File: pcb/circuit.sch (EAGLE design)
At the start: 148 parts, among them IC1 MCP1612-ADJI/MS, IC2 MCP73833-AMI/UN-ND, IC3 WE-TVS, IC4 MCP3423, IC5 ATWINC1510-MR210PB1952-ND, IC6 MAX3378EEUD, IC7 RN4870, IC8 ATSAML22N18A, J1 22-05-7038-03, J2 22-05-7038-03, Q1 ECX-1210, T1 PMOS, T10 NMOSSOT323, T11 NMOSSOT323, T12 NMOSSOT323, T2 NMOSSOT323, T3 NMOSSOT323, T4 NMOSSOT323, T5 NMOSSOT323, T6 NMOSSOT323, T7 NMOSSOT323, T8 NMOSSOT323, T9 NMOSSOT323, X1 USB2-MICRO, X10 2.5MM-AUDIO-JACK-MONONO_DRILL, X11 2.5MM-AUDIO-JACK-MONONO_DRILL, X12 2.5MM-AUDIO-JACK-MONONO_DRILL, X13 2.5MM-AUDIO-JACK-MONONO_DRILL, X14 MOLEX_1MM_FPC, X15 IGRID-20, X2 B3S-1000, X4 2.5MM-AUDIO-JACK-MONODRILL, X5 2.5MM-AUDIO-JACK-MONODRILL, X6 2.5MM-AUDIO-JACK-MONODRILL, X7 2.5MM-AUDIO-JACK-MONODRILL, X8 2.5MM-AUDIO-JACK-MONODRILL, X9 2.5MM-AUDIO-JACK-MONONO_DRILL

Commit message: routing finished
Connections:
- net SENSOR_IN_0: now also IC8.PB4; no longer IC8.PB5
- net SENSOR_IN_5: now also IC8.PB5; no longer IC8.PB4
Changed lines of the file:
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@@
 <net name="SENSOR_IN_0" class="0">
 <segment>
-<label x="48.26" y="111.76" size="0.889" layer="95" rot="R180" xref="yes"/>
-<pinref part="IC8" gate="G$1" pin="PB5"/>
-<wire x1="48.26" y1="111.76" x2="55.88" y2="111.76" width="0.1524" layer="91"/>
+<label x="48.26" y="114.3" size="0.889" layer="95" rot="R180" xref="yes"/>
+<wire x1="48.26" y1="114.3" x2="55.88" y2="114.3" width="0.1524" layer="91"/>
+<pinref part="IC8" gate="G$1" pin="PB4"/>
 </segment>
 </net>
@@
 <net name="SENSOR_IN_5" class="0">
 <segment>
-<label x="48.26" y="114.3" size="0.889" layer="95" rot="R180" xref="yes"/>
-<wire x1="48.26" y1="114.3" x2="55.88" y2="114.3" width="0.1524" layer="91"/>
-<pinref part="IC8" gate="G$1" pin="PB4"/>
+<label x="48.26" y="111.76" size="0.889" layer="95" rot="R180" xref="yes"/>
+<pinref part="IC8" gate="G$1" pin="PB5"/>
+<wire x1="48.26" y1="111.76" x2="55.88" y2="111.76" width="0.1524" layer="91"/>
 </segment>
 </net>

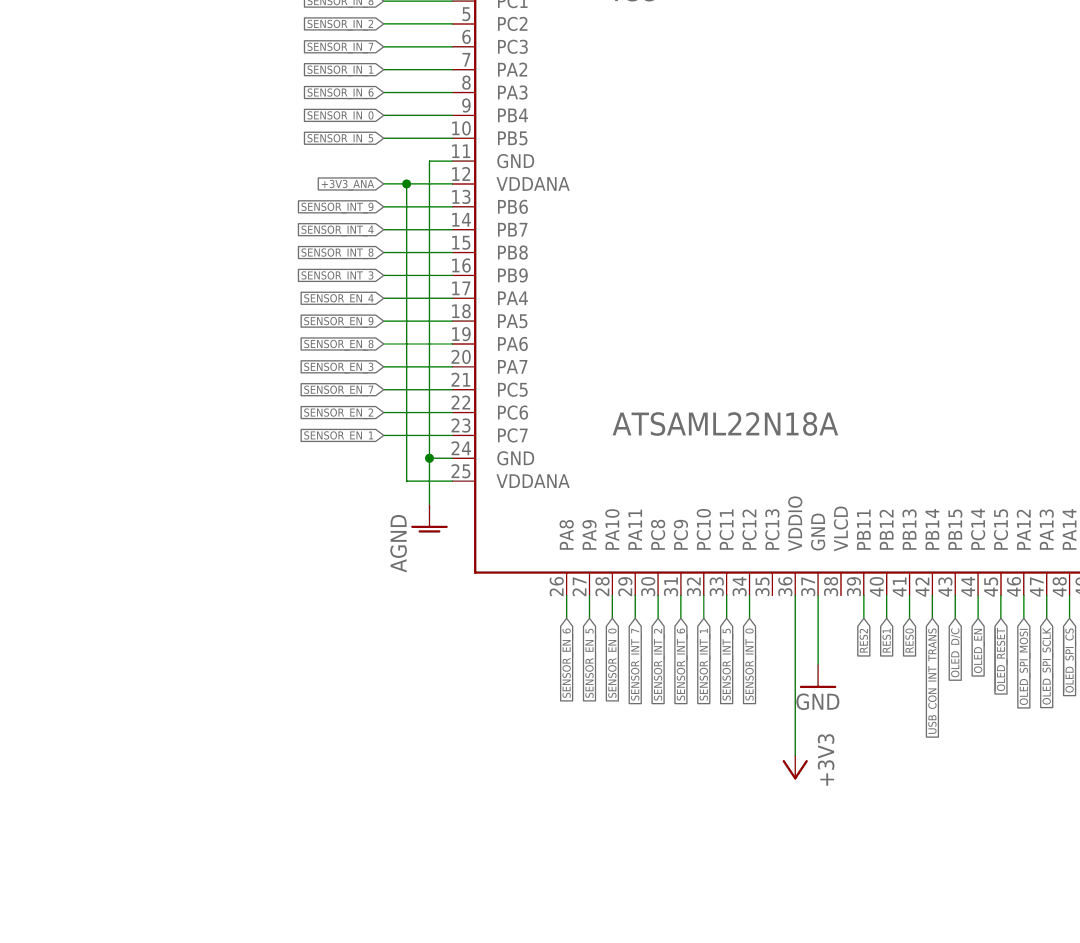
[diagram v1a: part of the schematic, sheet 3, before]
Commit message: Added Internal NTC
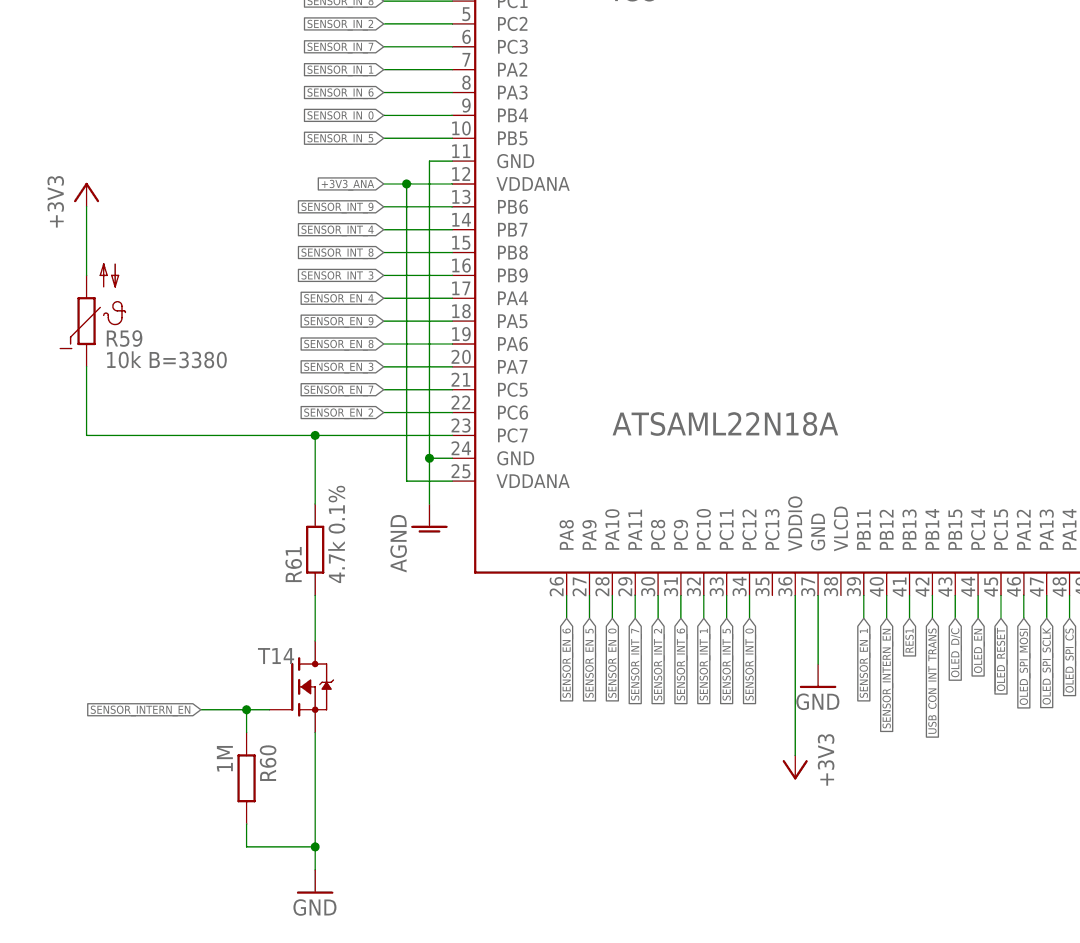
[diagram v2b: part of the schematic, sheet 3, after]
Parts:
- removed J1: 22-05-7038-03, con-molex:22-05-7038-03
- removed JP5: (no value), thermo:JP3
- added J3: 22-05-7048-04, con-molex:22-05-7048-04
- added JP2: (no value), thermo:JP3
- added R58: 100k, rcl:R-EU_R0603
- added R59: 10k B=3380, thermo:NTC-0603
- added R60: 1M, rcl:R-EU_R0603
- added R61: 4.7k 0.1%, rcl:R-EU_R0603
- added T13: PMOS, thermo:PMOS
- added T14: NMOSSOT323, thermo:NMOSSOT323
- JP8: device thermo:JP3 -> thermo:JP2
- T10, T11, T12, T2, T3, T4, T5, T6, T7, T8, T9: device Thermo_Library:NMOSSOT323 -> thermo:NMOSSOT323; OC_MOUSER 726-SP000917562 -> (none)
- renumbered U$1 to X3
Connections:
- removed net RES0: IC8.PB13, JP5.1
- removed net RES2: IC8.PB11, JP5.3
- removed net VIN: JP7.2
- new net SENSOR_INTERN_DRAIN: R61.1, T14.D
- new net SENSOR_INTERN_EN: IC8.PB12, JP8.1, R60.1, T14.G
- new net SENSOR_INTERN_IN: IC8.PC7, R59.1, R61.2
- new net VAT_EN: R58.2, T13.G
- new net VBAT_UNPROT: J3-1.S, T13.D
- net !OLED_SPI_CS: now also JP2.3; no longer JP8.3
- net +3V3: now also JP7.2, R59.2
- net CHARGER_NTC: now also J3-2.S; no longer J1-2.S
- net GND: now also J3-3.S, J3-4.S, R58.1, R60.2, T14.S; no longer J1-3.S
- net OLED_SPI_MOSI: now also JP2.1; no longer JP8.1
- net OLED_SPI_SCLK: now also JP2.2; no longer JP8.2
- net RES1: now also IC8.PB13, JP8.2; no longer IC8.PB12, JP5.2
- net SENSOR_EN_1: now also IC8.PB11; no longer IC8.PC7
- net VBAT: now also T13.S; no longer J1-1.S
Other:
- moved on the sheet: R32, R33
